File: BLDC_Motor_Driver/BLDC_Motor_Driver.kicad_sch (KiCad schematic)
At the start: 41 parts, among them J101 Conn_01x08, J102 395221002, J103 USB4105-GF-A, J104 Conn_01x05, J105 Conn_01x05, J106 Conn_01x04, J107 395221005, J108 395221003, J109 Conn_02x12_Counter_Clockwise, J110 395221005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

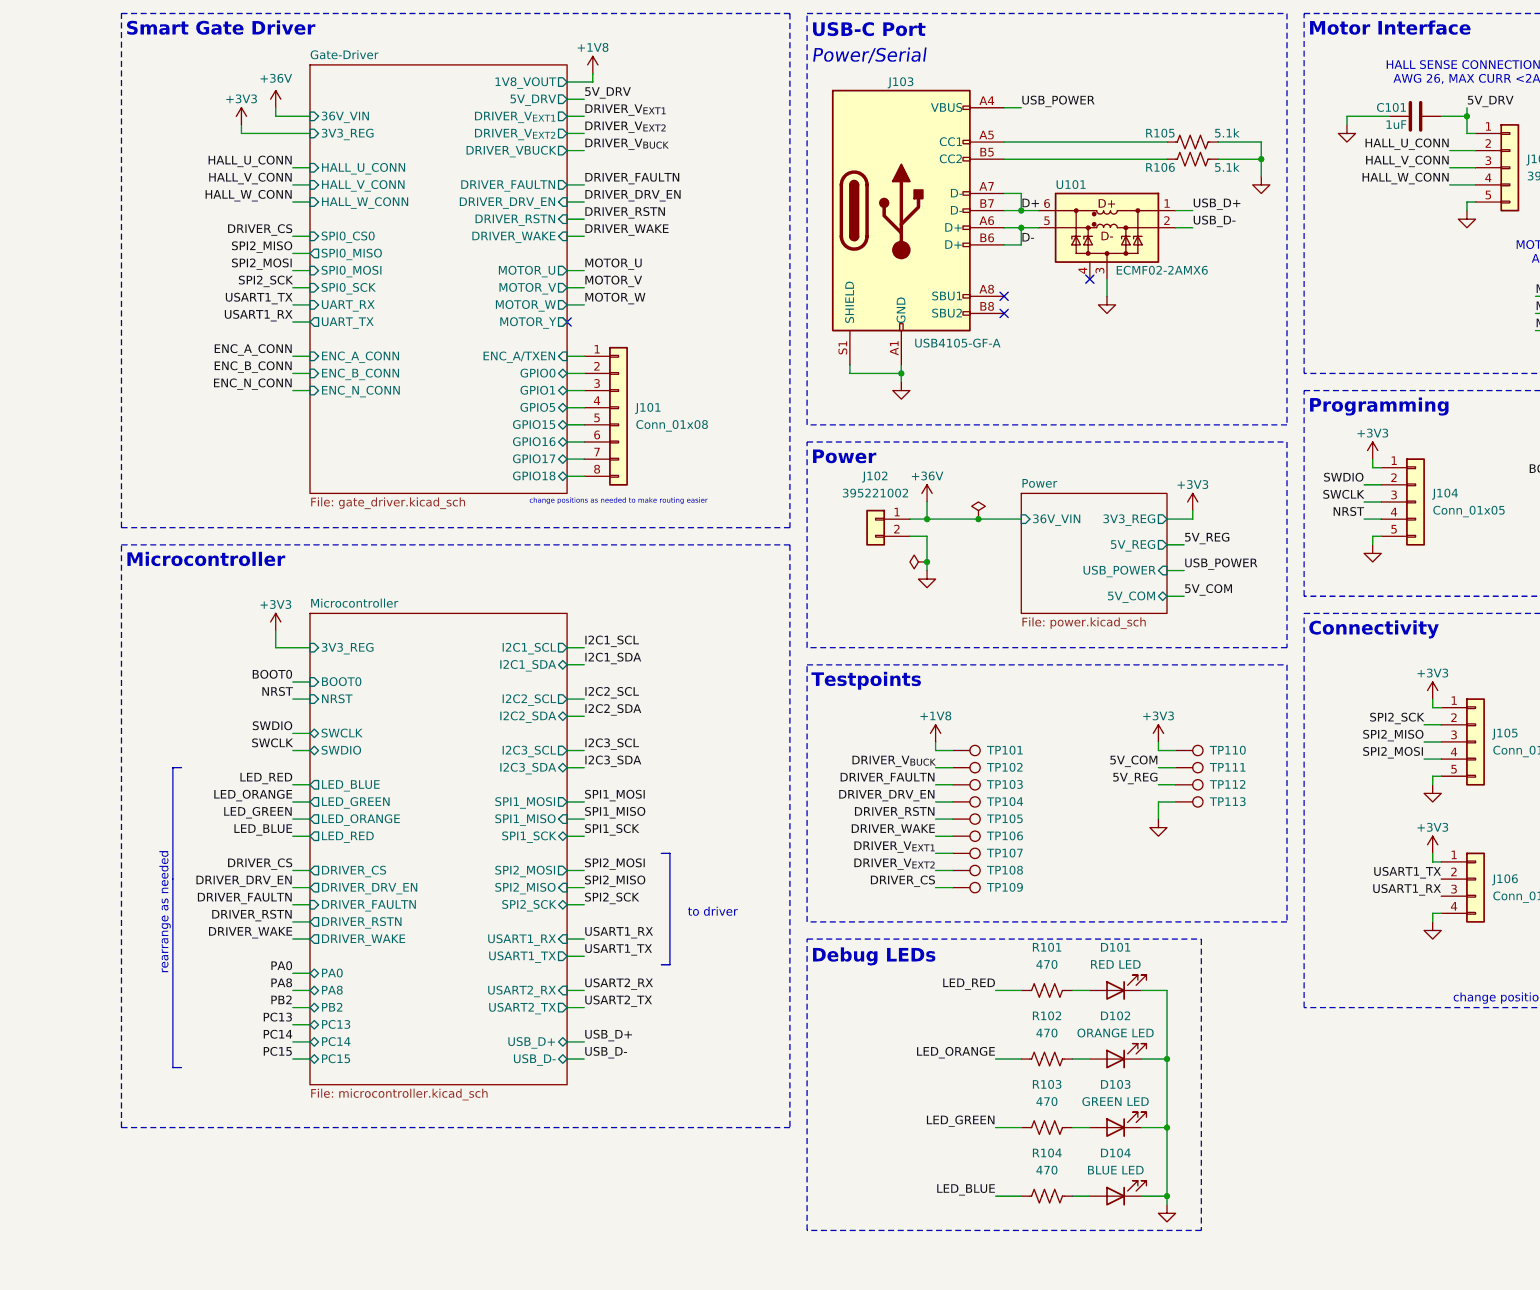
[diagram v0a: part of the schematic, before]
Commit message: move elements to logical regions
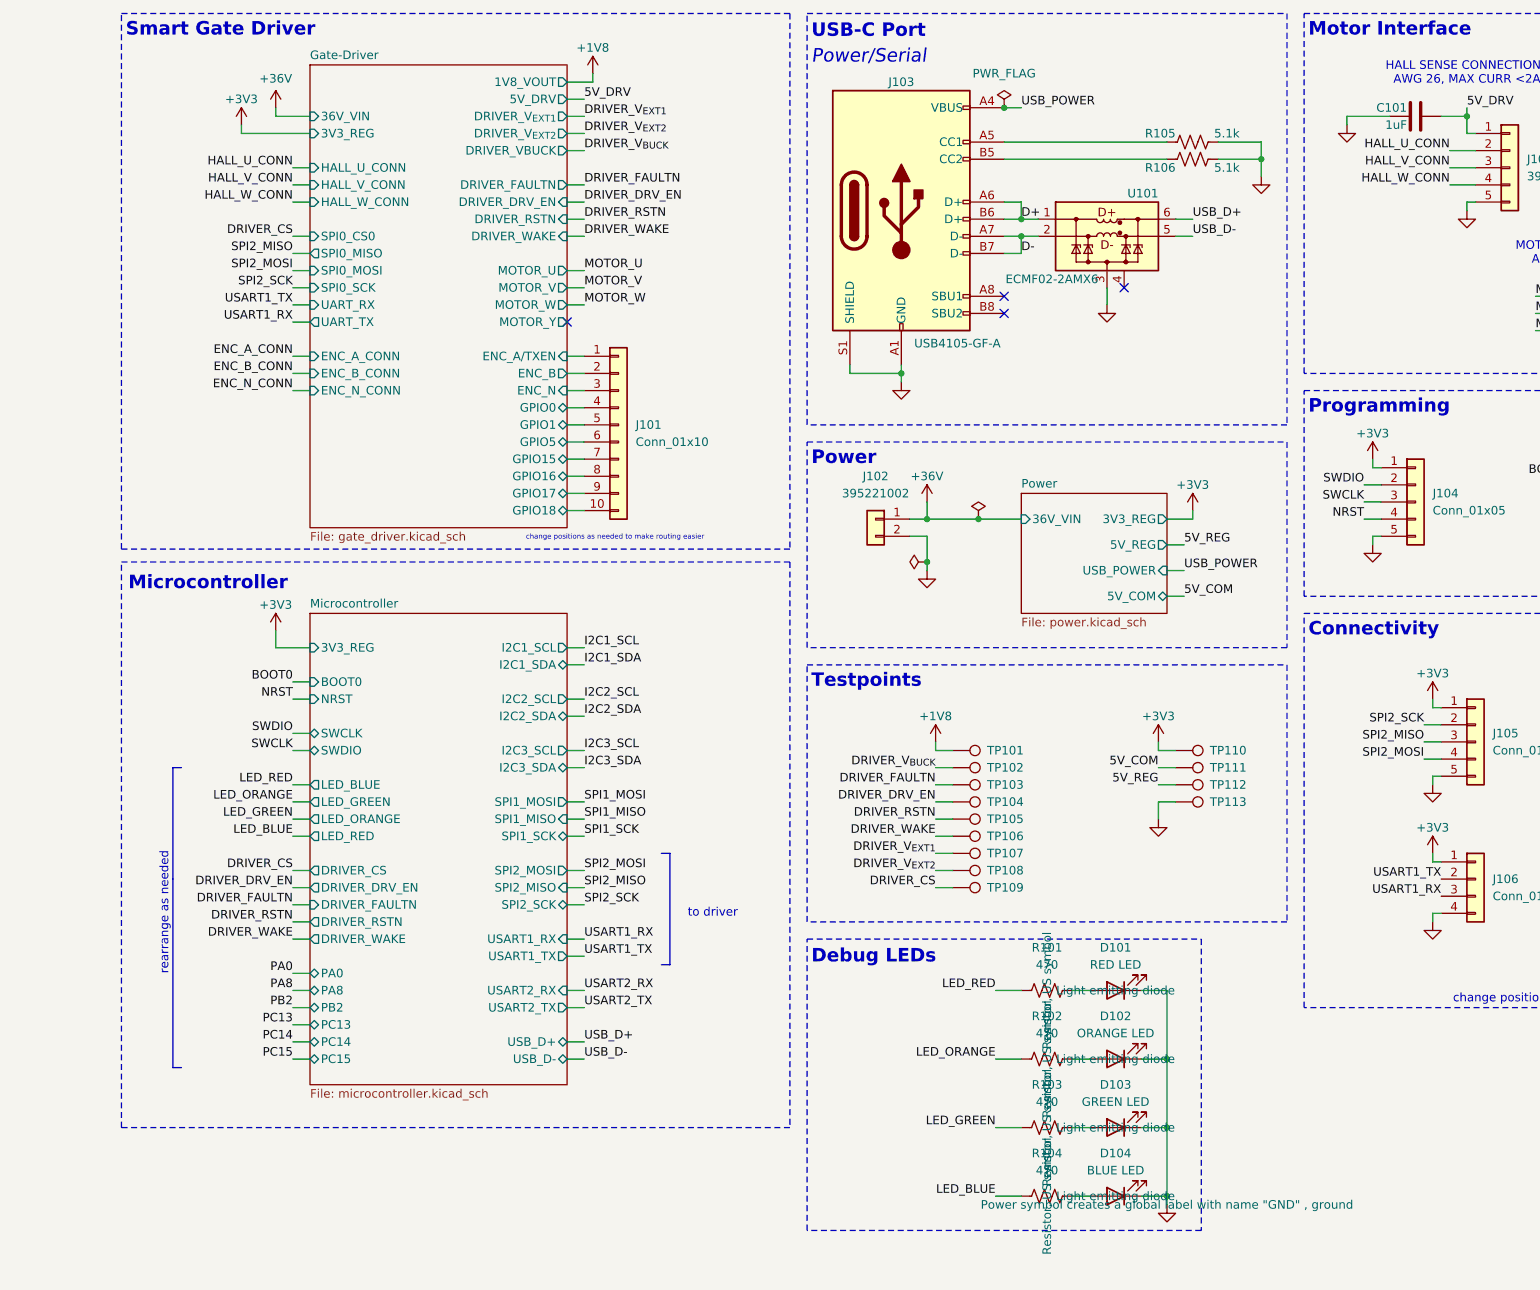
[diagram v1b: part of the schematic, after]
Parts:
- removed J101: Conn_01x08, Connector_PinHeader_2.54mm:PinHeader_1x08_P2.54mm_Vertical, symbol Connector_Generic:Conn_01x08
- added J101: Conn_01x10, Connector_PinHeader_2.54mm:PinHeader_1x10_P2.54mm_Vertical, symbol Connector_Generic:Conn_01x10
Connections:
- net D+: now also J103.A6 (D+), J103.B6 (D+), U101.1 (D+_in); no longer J103.A7 (D-), J103.B7 (D-), U101.6 (D+_out)
- net D-: now also J103.A7 (D-), J103.B7 (D-), U101.2 (D-_in); no longer J103.A6 (D+), J103.B6 (D+), U101.5 (D-_out)
- net Gate-Driver/ENC_A/TXEN: now also J101.1 (Pin_1)
- net Gate-Driver/GPIO0: now also J101.4 (Pin_4)
- net Gate-Driver/GPIO1: now also J101.5 (Pin_5)
- net Gate-Driver/GPIO15: now also J101.7 (Pin_7)
- net Gate-Driver/GPIO16: now also J101.8 (Pin_8)
- net Gate-Driver/GPIO17: now also J101.9 (Pin_9)
- net Gate-Driver/GPIO18: now also J101.10 (Pin_10)
- net Gate-Driver/GPIO5: now also J101.6 (Pin_6)
- net USB_D+: now also U101.6 (D+_out); no longer U101.1 (D+_in)
- net USB_D-: now also U101.5 (D-_out); no longer U101.2 (D-_in)
- new net Gate-Driver/ENC_B: J101.2 (Pin_2)
- new net Gate-Driver/ENC_N: J101.3 (Pin_3)
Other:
- sheet Gate-Driver ports: added ENC_B, ENC_N; removed none
- moved on the sheet: U101

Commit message: removed unnecessary Y phase. finished Motor Conn Layout
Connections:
- net HALL_U_CONN: now also J107.4 (Pin_4); no longer J107.2 (Pin_2)
- net HALL_W_CONN: now also J107.2 (Pin_2); no longer J107.4 (Pin_4)
- net MOTOR_U: now also J108.3 (Pin_3); no longer J108.1 (Pin_1)
- net MOTOR_W: now also J108.1 (Pin_1); no longer J108.3 (Pin_3)
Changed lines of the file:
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@@
 		)
 	)
-	(label "MOTOR_W"
+	(label "MOTOR_U"
 		(at 224.79 62.23 0)
 		(effects
@@
 		)
 	)
-	(label "HALL_U_CONN"
+	(label "HALL_W_CONN"
 		(at 212.09 35.56 180)
 		(effects
@@
 		)
 	)
-	(label "HALL_W_CONN"
+	(label "HALL_U_CONN"
 		(at 212.09 40.64 180)
 		(effects
@@
 		)
 	)
-	(label "MOTOR_U"
+	(label "MOTOR_W"
 		(at 224.79 57.15 0)
 		(effects

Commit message: board outline, most component placements, routed driver and some other stuff
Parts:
- added H101, H102, H103, H104: M3, MountingHole:MountingHole_3.2mm_M3_Pad_Via, symbol Mechanical:MountingHole_Pad
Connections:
- net D+: now also U101.6 (D+_out); no longer U101.1 (D+_in)
- net D-: now also U101.5 (D-_out); no longer U101.2 (D-_in)
- net USART1_RX: now also J106.2 (Pin_2); no longer J106.3 (Pin_3)
- net USART1_TX: now also J106.3 (Pin_3); no longer J106.2 (Pin_2)
- net USB_D+: now also U101.1 (D+_in); no longer U101.6 (D+_out)
- net USB_D-: now also U101.2 (D-_in); no longer U101.5 (D-_out)
- no-connect marks 5 -> 9
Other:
- note added: "Mounting Holes"

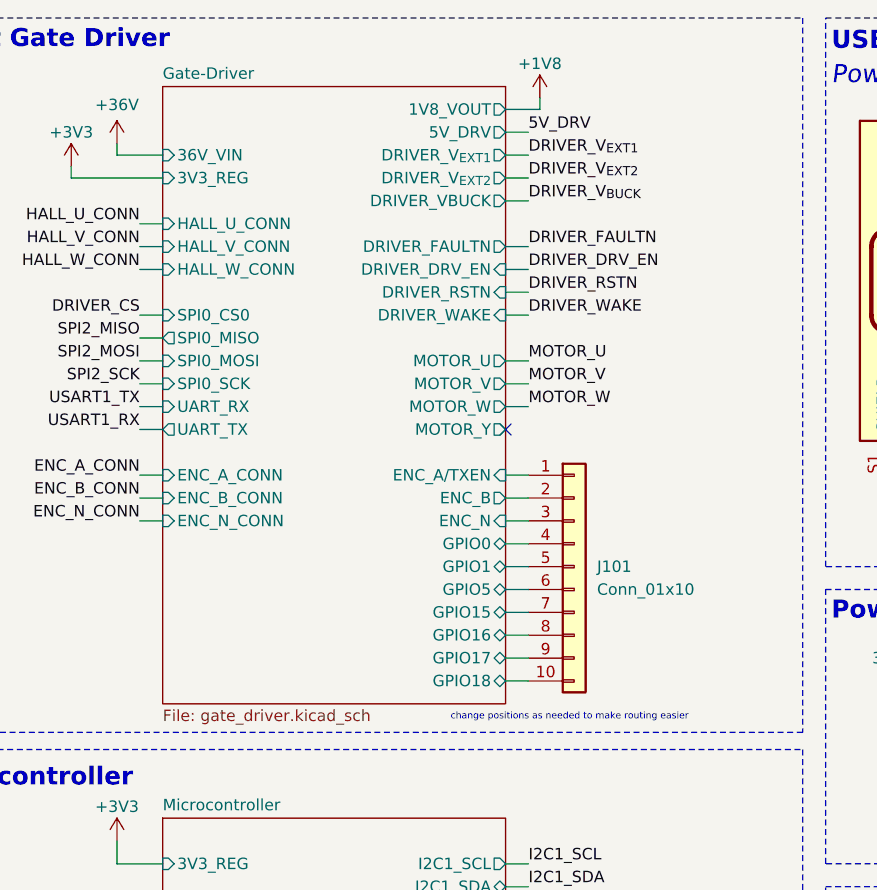
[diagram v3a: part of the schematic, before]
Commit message: most power routing done
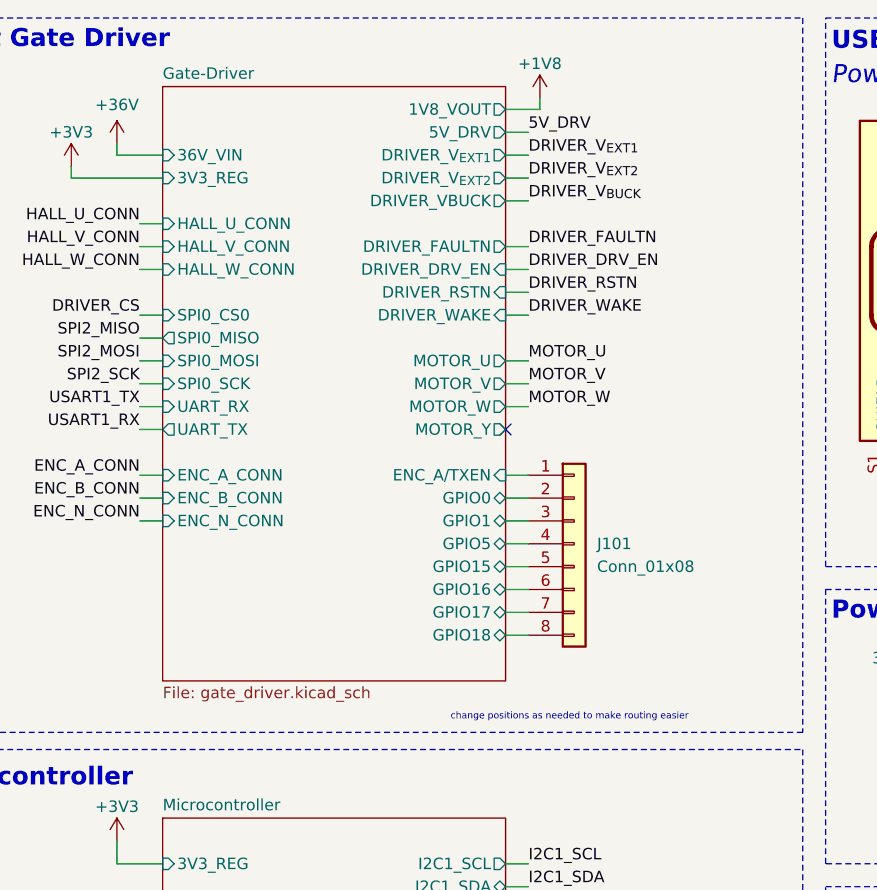
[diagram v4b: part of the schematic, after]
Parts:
- J101: value Conn_01x10 -> Conn_01x08; footprint Connector_PinHeader_2.54mm:PinHeader_1x10_P2.54mm_Vertical -> Connector_PinHeader_2.54mm:PinHeader_1x08_P2.54mm_Vertical; symbol Connector_Generic:Conn_01x10 -> Connector_Generic:Conn_01x08
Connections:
- net Gate-Driver/ENC_B is gone; now on net Gate-Driver/GPIO0: J101.2 (Pin_2)
- net Gate-Driver/ENC_N is gone; now on net Gate-Driver/GPIO1: J101.3 (Pin_3)
- net Gate-Driver/GPIO0: no longer J101.4 (Pin_4)
- net Gate-Driver/GPIO1: no longer J101.5 (Pin_5)
- net Gate-Driver/GPIO15: now also J101.5 (Pin_5); no longer J101.7 (Pin_7)
- net Gate-Driver/GPIO16: now also J101.6 (Pin_6); no longer J101.8 (Pin_8)
- net Gate-Driver/GPIO17: now also J101.7 (Pin_7); no longer J101.9 (Pin_9)
- net Gate-Driver/GPIO18: now also J101.8 (Pin_8); no longer J101.10 (Pin_10)
- net Gate-Driver/GPIO5: now also J101.4 (Pin_4); no longer J101.6 (Pin_6)
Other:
- sheet Gate-Driver ports: added none; removed ENC_B, ENC_N
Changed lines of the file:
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@@
 	(wire
 		(pts
-			(xy 81.28 30.48) (xy 83.82 30.48)
+			(xy 81.28 66.04) (xy 83.82 66.04)
 		)
 		(stroke
@@
 	(wire
 		(pts
-			(xy 135.89 137.16) (xy 138.43 137.16)
+			(xy 81.28 30.48) (xy 83.82 30.48)
 		)
 		(stroke
@@
 	(wire
 		(pts
-			(xy 81.28 33.02) (xy 83.82 33.02)
+			(xy 135.89 137.16) (xy 138.43 137.16)
 		)
 		(stroke
@@
 	(wire
 		(pts
-			(xy 264.16 132.08) (xy 261.62 132.08)
+			(xy 81.28 33.02) (xy 83.82 33.02)
 		)
 		(stroke
@@
 	(wire
 		(pts
-			(xy 254 33.02) (xy 255.27 33.02)
+			(xy 264.16 132.08) (xy 261.62 132.08)
 		)
 		(stroke
@@
 	(wire
 		(pts
-			(xy 246.38 121.92) (xy 248.92 121.92)
+			(xy 254 33.02) (xy 255.27 33.02)
 		)
 		(stroke
@@
 	(wire
 		(pts
-			(xy 81.28 76.2) (xy 83.82 76.2)
+			(xy 246.38 121.92) (xy 248.92 121.92)
 		)
 		(stroke
@@
 	(wire
 		(pts
-			(xy 81.28 78.74) (xy 83.82 78.74)
-		)
-		(stroke
-			(width 0)
-			(type default)
-		)
-	)
-	(wire
-		(pts
 			(xy 246.38 132.08) (xy 248.92 132.08)
 		)
@@
 	(wire
 		(pts
-			(xy 81.28 88.9) (xy 83.82 88.9)
-		)
-		(stroke
-			(width 0)
-			(type default)
-		)
-	)
-	(wire
-		(pts
 			(xy 33.02 31.75) (xy 33.02 33.02)
 		)
@@
 	(wire
 		(pts
+			(xy 81.28 73.66) (xy 83.82 73.66)
+		)
+		(stroke
+			(width 0)
+			(type default)
+		)
+	)
+	(wire
+		(pts
 			(xy 135.89 127) (xy 138.43 127)
 		)
@@
 	(wire
 		(pts
-			(xy 81.28 83.82) (xy 83.82 83.82)
-		)
-		(stroke
-			(width 0)
-			(type default)
-		)
-	)
-	(wire
-		(pts
 			(xy 81.28 162.56) (xy 83.82 162.56)
 		)
@@
 	(wire
 		(pts
-			(xy 81.28 71.12) (xy 83.82 71.12)
-		)
-		(stroke
-			(width 0)
-			(type default)
-		)
-	)
-	(wire
-		(pts
 			(xy 40.64 66.04) (xy 43.18 66.04)
 		)
@@
 	(wire
 		(pts
-			(xy 81.28 73.66) (xy 83.82 73.66)
-		)
-		(stroke
-			(width 0)
-			(type default)
-		)
-	)
-	(wire
-		(pts
 			(xy 40.64 149.86) (xy 43.18 149.86)
 		)
@@
 	(wire
 		(pts
+			(xy 81.28 76.2) (xy 83.82 76.2)
+		)
+		(stroke
+			(width 0)
+			(type default)
+		)
+	)
+	(wire
+		(pts
 			(xy 38.1 30.48) (xy 43.18 30.48)
 		)
@@
 	(wire
 		(pts
+			(xy 81.28 78.74) (xy 83.82 78.74)
+		)
+		(stroke
+			(width 0)
+			(type default)
+		)
+	)
+	(wire
+		(pts
 			(xy 146.05 43.18) (xy 148.59 43.18)
 		)
@@
 	(wire
 		(pts
+			(xy 81.28 68.58) (xy 83.82 68.58)
+		)
+		(stroke
+			(width 0)
+			(type default)
+		)
+	)
+	(wire
+		(pts
 			(xy 254 30.48) (xy 254 33.02)
 		)
@@
 	(wire
 		(pts
-			(xy 81.28 66.04) (xy 83.82 66.04)
+			(xy 81.28 71.12) (xy 83.82 71.12)
 		)
 		(stroke
@@
 	(wire
 		(pts
+			(xy 81.28 81.28) (xy 83.82 81.28)
+		)
+		(stroke
+			(width 0)
+			(type default)
+		)
+	)
+	(wire
+		(pts
 			(xy 83.82 170.18) (xy 81.28 170.18)
 		)
@@
 	(wire
 		(pts
-			(xy 81.28 68.58) (xy 83.82 68.58)
-		)
-		(stroke
-			(width 0)
-			(type default)
-		)
-	)
-	(wire
-		(pts
 			(xy 224.79 59.69) (xy 234.95 59.69)
 		)
@@
 	(wire
 		(pts
-			(xy 81.28 86.36) (xy 83.82 86.36)
-		)
-		(stroke
-			(width 0)
-			(type default)
-		)
-	)
-	(wire
-		(pts
 			(xy 83.82 109.22) (xy 81.28 109.22)
 		)
@@
 	(wire
 		(pts
-			(xy 81.28 81.28) (xy 83.82 81.28)
+			(xy 233.68 83.82) (xy 233.68 90.17)
 		)
 		(stroke
@@
 	(wire
 		(pts
-			(xy 233.68 83.82) (xy 233.68 90.17)
+			(xy 177.8 36.83) (xy 184.15 36.83)
 		)
 		(stroke
@@
 	(wire
 		(pts
-			(xy 177.8 36.83) (xy 184.15 36.83)
+			(xy 40.64 144.78) (xy 43.18 144.78)
 		)
 		(stroke
@@
 	(wire
 		(pts
-			(xy 40.64 144.78) (xy 43.18 144.78)
+			(xy 130.81 68.58) (xy 130.81 69.85)
 		)
 		(stroke
@@
 	(wire
 		(pts
-			(xy 130.81 68.58) (xy 130.81 69.85)
+			(xy 81.28 35.56) (xy 83.82 35.56)
 		)
 		(stroke
@@
 	(wire
 		(pts
-			(xy 81.28 35.56) (xy 83.82 35.56)
+			(xy 81.28 83.82) (xy 83.82 83.82)
 		)
 		(stroke
@@
 	)
 	(symbol
-		(lib_id "Connector_Generic:Conn_01x10")
-		(at 88.9 76.2 0)
+		(lib_id "Connector_Generic:Conn_01x08")
+		(at 88.9 73.66 0)
 		(unit 1)
 		(exclude_from_sim no)
@@
 		(fields_autoplaced yes)
 		(property "Reference" "J101"
-			(at 91.44 76.1999 0)
+			(at 91.44 73.6599 0)
 			(effects
 				(font
@@
 			)
 		)
-		(property "Value" "Conn_01x10"
-			(at 91.44 78.7399 0)
+		(property "Value" "Conn_01x08"
+			(at 91.44 76.1999 0)
 			(effects
 				(font
@@
 			)
 		)
-		(property "Footprint" "Connector_PinHeader_2.54mm:PinHeader_1x10_P2.54mm_Vertical"
-			(at 88.9 76.2 0)
+		(property "Footprint" "Connector_PinHeader_2.54mm:PinHeader_1x08_P2.54mm_Vertical"
+			(at 88.9 73.66 0)
 			(effects
 				(font
@@
 		)
 		(property "Datasheet" "~"
-			(at 88.9 76.2 0)
+			(at 88.9 73.66 0)
 			(effects
 				(font
@@
 			)
 		)
-		(property "Description" "Generic connector, single row, 01x10, script generated (kicad-library-utils/schlib/autogen/connector/)"
-			(at 88.9 76.2 0)
+		(property "Description" "Generic connector, single row, 01x08, script generated (kicad-library-utils/schlib/autogen/connector/)"
+			(at 88.9 73.66 0)
 			(effects
 				(font
@@
 			)
 		)
-		(pin "9"
-		)
 		(pin "5"
 		)
@@
 		(pin "7"
 		)
-		(pin "10"
-		)
 		(instances
 			(project ""
@@
 	(sheet
 		(at 43.18 22.86)
-		(size 38.1 68.58)
+		(size 38.1 66.04)
 		(exclude_from_sim no)
 		(in_bom yes)
@@
 		)
 		(property "Sheetfile" "gate_driver.kicad_sch"
-			(at 43.18 92.0246 0)
+			(at 43.18 89.4846 0)
 			(effects
 				(font
@@
 		)
 		(pin "GPIO0" bidirectional
-			(at 81.28 73.66 0)
+			(at 81.28 68.58 0)
 			(effects
 				(font
@@
 		)
 		(pin "GPIO1" bidirectional
-			(at 81.28 76.2 0)
+			(at 81.28 71.12 0)
 			(effects
 				(font
@@
 		)
 		(pin "GPIO5" bidirectional
-			(at 81.28 78.74 0)
+			(at 81.28 73.66 0)
 			(effects
 				(font
@@
 		)
 		(pin "GPIO15" bidirectional
-			(at 81.28 81.28 0)
+			(at 81.28 76.2 0)
 			(effects
 				(font
@@
 		)
 		(pin "GPIO16" bidirectional
-			(at 81.28 83.82 0)
+			(at 81.28 78.74 0)
 			(effects
 				(font
@@
 		)
 		(pin "GPIO17" bidirectional
-			(at 81.28 86.36 0)
+			(at 81.28 81.28 0)
 			(effects
 				(font
@@
 		)
 		(pin "GPIO18" bidirectional
-			(at 81.28 88.9 0)
+			(at 81.28 83.82 0)
 			(effects
 				(font
@@
 			)
 		)
-		(pin "ENC_B" output
-			(at 81.28 68.58 0)
-			(effects
-				(font
-					(size 1.27 1.27)
-				)
-				(justify right)
-			)
-		)
-		(pin "ENC_N" input
-			(at 81.28 71.12 0)
-			(effects
-				(font
-					(size 1.27 1.27)
-				)
-				(justify right)
-			)
-		)
